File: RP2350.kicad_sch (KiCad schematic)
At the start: 32 parts, among them SW1 SW_Push, SW2 SW_Push, U1 RP2350A, U4 AMS1117-3.3, U5 ABM8-272-T3_C20625731

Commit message: worked on some shit
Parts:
- added Debug: Conn_01x03_Pin, Connector_PinHeader_2.54mm:PinHeader_1x03_P2.54mm_Vertical, symbol Connector:Conn_01x03_Pin
- added R11: 1k, Resistor_SMD:R_0805_2012Metric_Pad1.20x1.40mm_HandSolder, symbol Device:R
- added SW3: SW_Push, Button_Switch_SMD:SW_SPST_EVQPE1, symbol Switch:SW_Push
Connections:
- net BOOT: now also R11.1
- net GND: now also Debug.2 (Pin_2), SW3.1
- net XOUT: now also C9.1
- net SWCLK: now reaches U1.24 (SWCLK)
- net SWCLK: now also Debug.1 (Pin_1)
- net SWDIO: now reaches U1.25 (SWDIO)
- net SWDIO: now also Debug.3 (Pin_3)
- new net: R11.2, SW3.2
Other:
- note added: "Boot"
- note added: "Osc"
- note added: "Reset"
- moved on the sheet: C10, C7, C9, R4, R5, SW1, SW2, U5

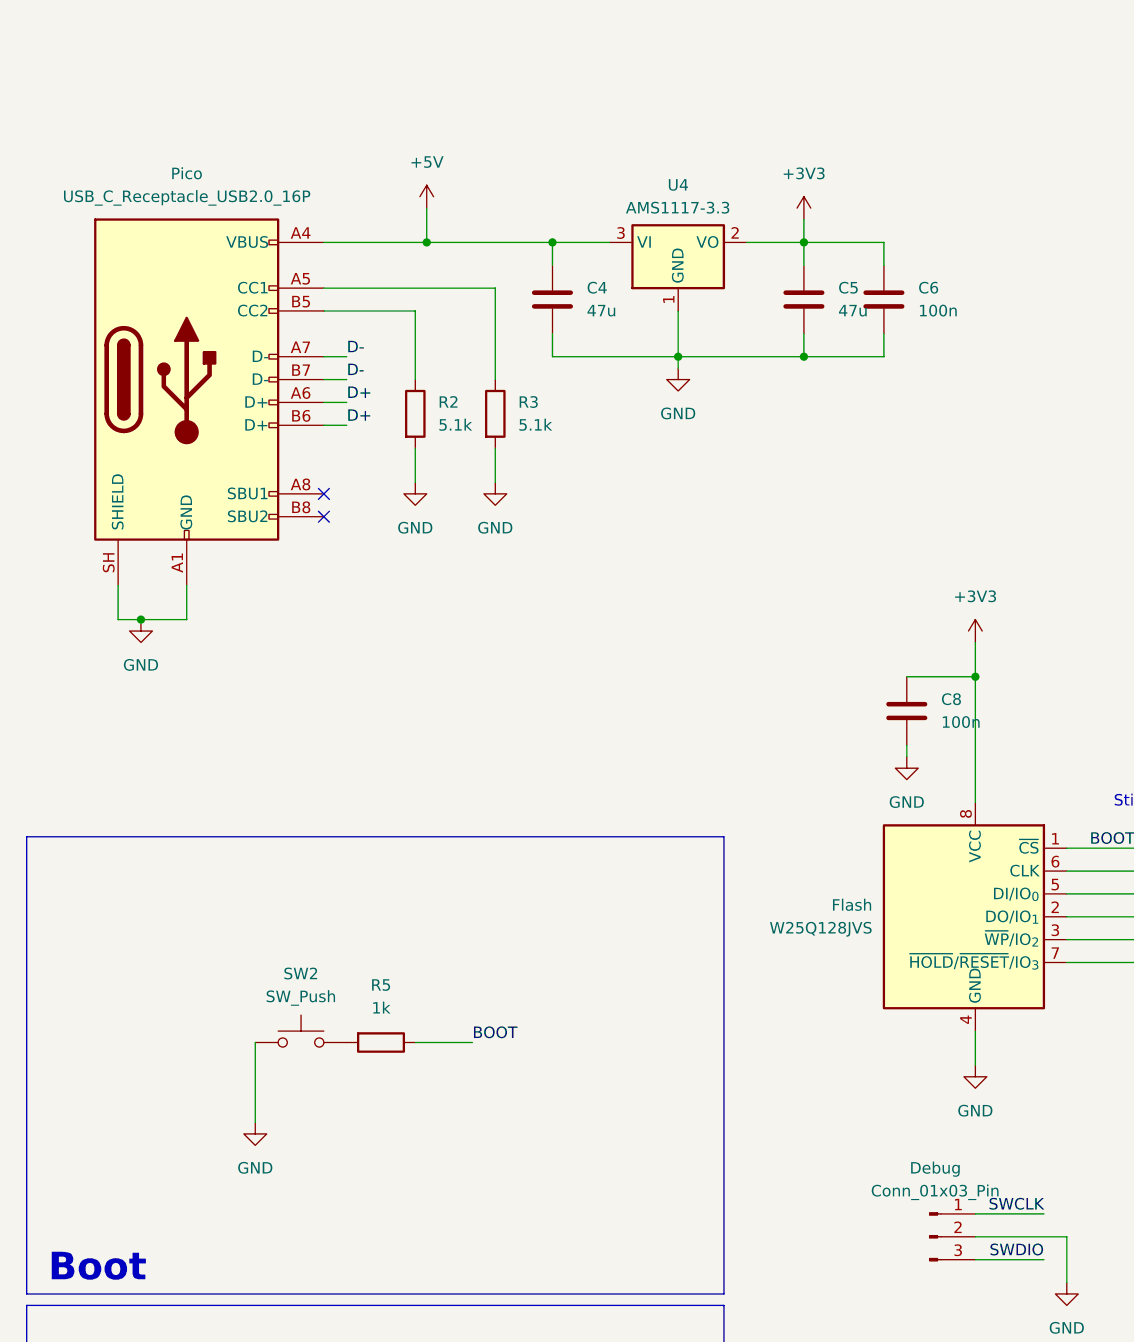
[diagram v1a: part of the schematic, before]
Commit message: added some lcsc part numbers
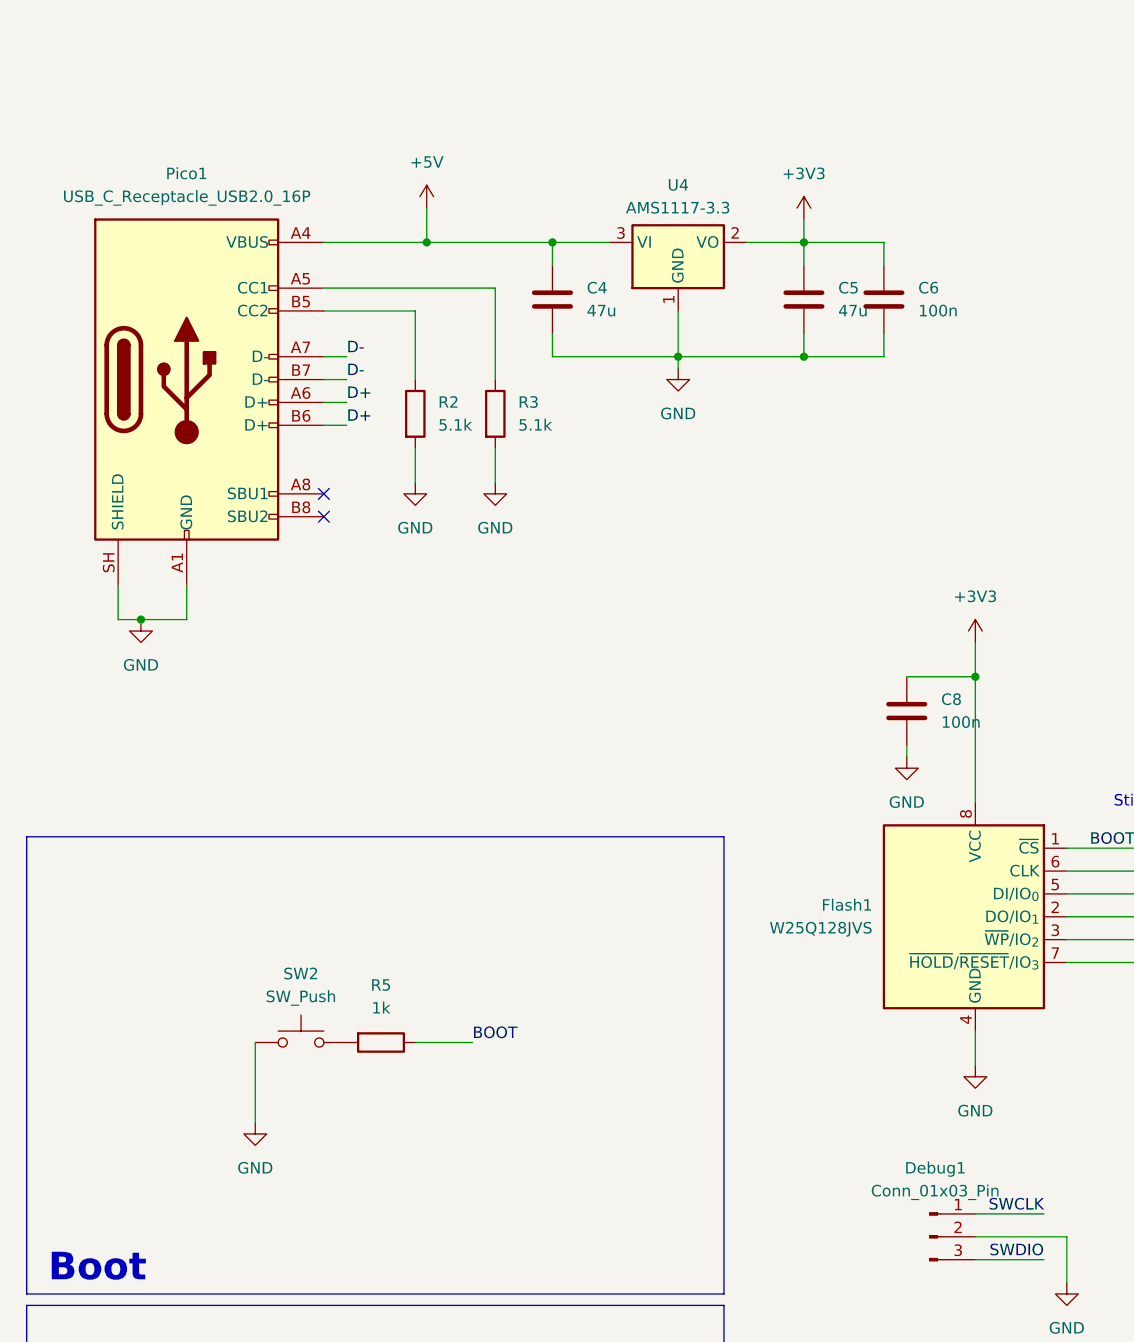
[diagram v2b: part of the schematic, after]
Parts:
- renumbered Debug to Debug1, Flash to Flash1, Pico to Pico1
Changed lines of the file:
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@@
 		(in_pos_files yes)
 		(dnp no)
-		(property "Reference" "Flash"
+		(property "Reference" "Flash1"
 			(at 106.68 101.5999 0)
 			(show_name no)
@@
 			(project "TheDevBoard"
 				(path "/962e0ac6-7545-4a58-b6cb-cae1d23e787f/83027dc2-8dcc-4189-b732-ecb78df2ee53"
-					(reference "Flash")
+					(reference "Flash1")
 					(unit 1)
 				)
@@
 		(dnp no)
 		(fields_autoplaced yes)
-		(property "Reference" "Debug"
+		(property "Reference" "Debug1"
 			(at 113.665 130.81 0)
 			(show_name no)
@@
 			(project "TheDevBoard"
 				(path "/962e0ac6-7545-4a58-b6cb-cae1d23e787f/83027dc2-8dcc-4189-b732-ecb78df2ee53"
-					(reference "Debug")
+					(reference "Debug1")
 					(unit 1)
 				)
@@
 		(dnp no)
 		(fields_autoplaced yes)
-		(property "Reference" "Pico"
+		(property "Reference" "Pico1"
 			(at 30.48 20.32 0)
 			(show_name no)
@@
 			(project "TheDevBoard"
 				(path "/962e0ac6-7545-4a58-b6cb-cae1d23e787f/83027dc2-8dcc-4189-b732-ecb78df2ee53"
-					(reference "Pico")
+					(reference "Pico1")
 					(unit 1)
 				)

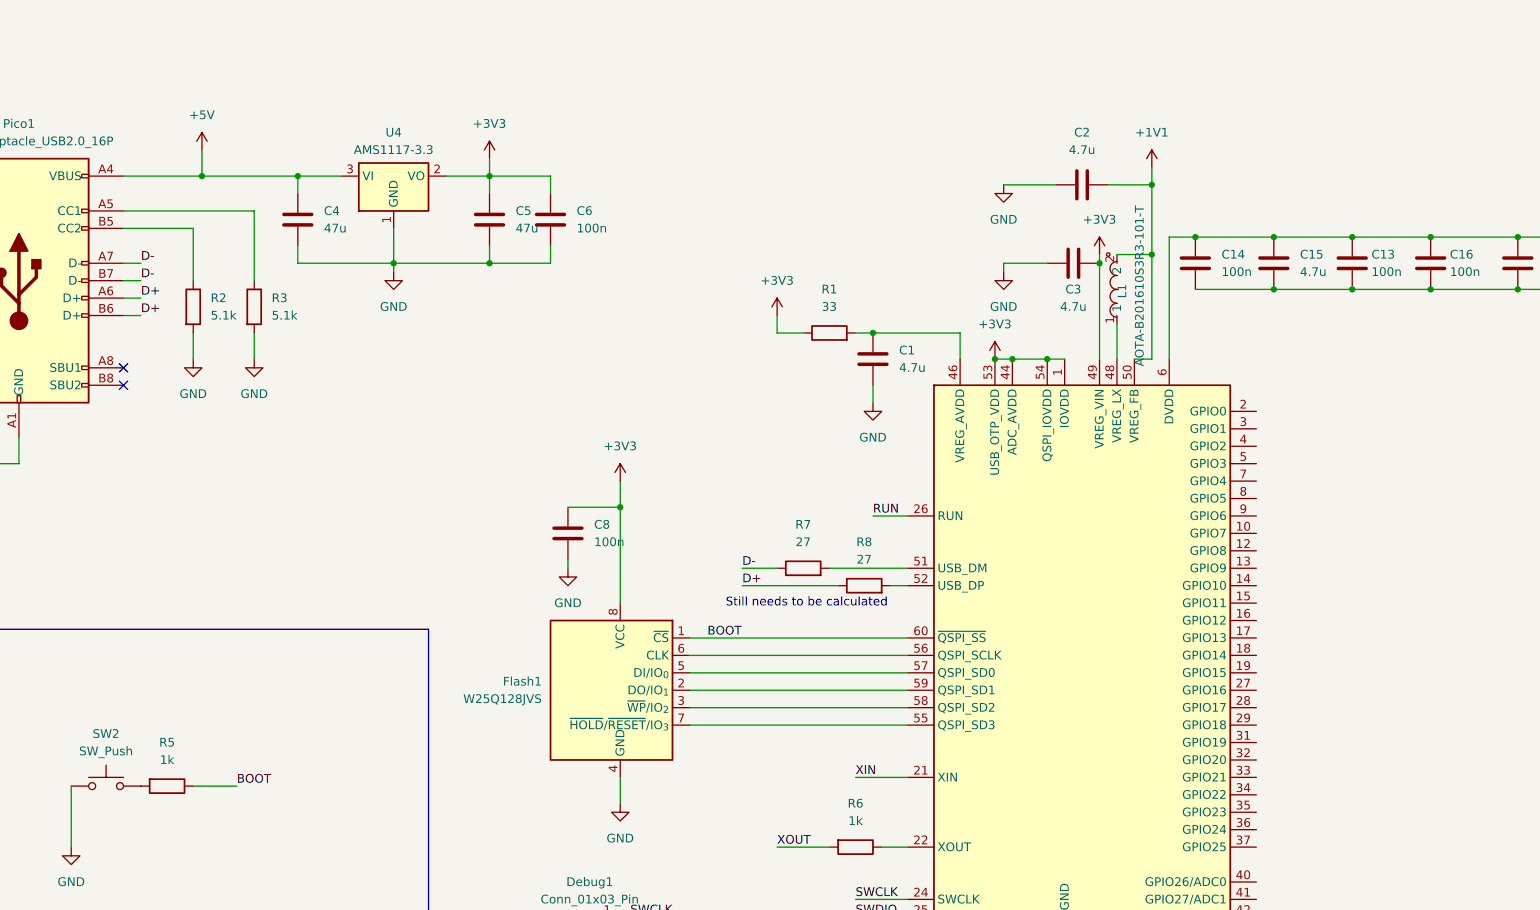
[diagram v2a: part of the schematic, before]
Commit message: created esp32 s3 mini connection to rp2350 added SD card Routed them together
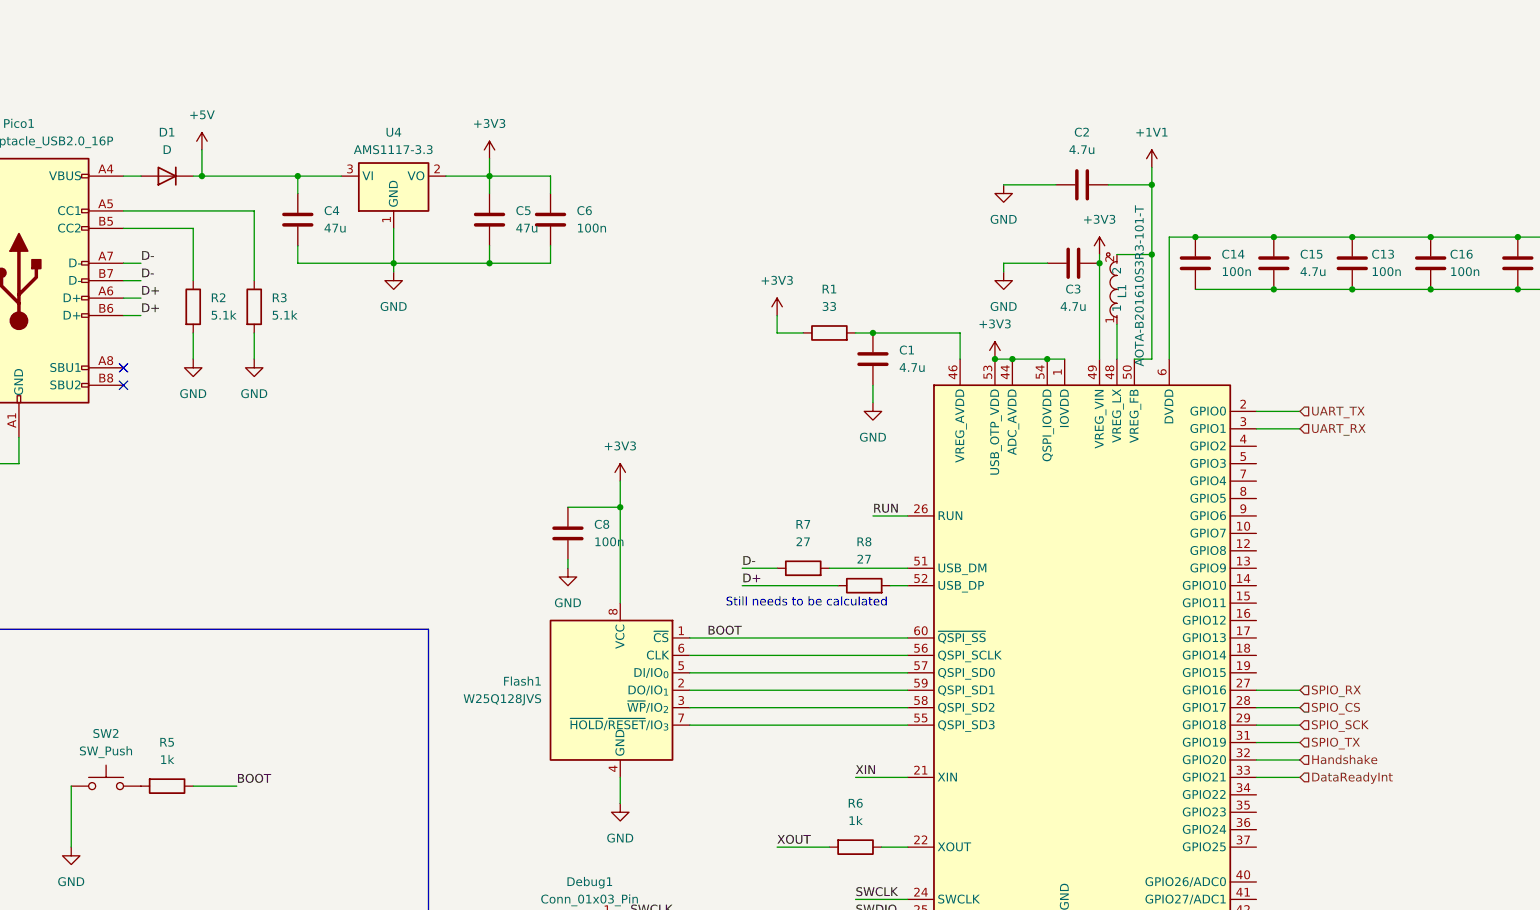
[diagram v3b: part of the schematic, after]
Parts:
- added D1: D, Diode_SMD:D_0805_2012Metric, symbol Device:D
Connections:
- net +5V: now also D1.1 (K); no longer Pico1.A4 (VBUS), Pico1.A9 (VBUS), Pico1.B4 (VBUS), Pico1.B9 (VBUS)
- net UART_TX: now reaches U1.2 (GPIO0)
- net SPIO_RX: now reaches U1.27 (GPIO16)
- net SPIO_CS: now reaches U1.28 (GPIO17)
- net SPIO_SCK: now reaches U1.29 (GPIO18)
- net UART_RX: now reaches U1.3 (GPIO1)
- net SPIO_TX: now reaches U1.31 (GPIO19)
- net Handshake: now reaches U1.32 (GPIO20)
- net DataReadyInt: now reaches U1.33 (GPIO21)
- new net: D1.2 (A), Pico1.A4 (VBUS), Pico1.A9 (VBUS), Pico1.B4 (VBUS), Pico1.B9 (VBUS)

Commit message: generated pdf
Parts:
- removed C4, C5: 47u, Capacitor_SMD:C_0805_2012Metric_Pad1.18x1.45mm_HandSolder, symbol Device:C
- removed C6: 100n, Capacitor_SMD:C_0805_2012Metric_Pad1.18x1.45mm_HandSolder, symbol Device:C
- removed R11: 1k, Resistor_SMD:R_0805_2012Metric_Pad1.20x1.40mm_HandSolder, symbol Device:R
- removed SW3: SW_Push, Button_Switch_SMD:SW_SPST_EVQPE1, symbol Switch:SW_Push
- removed U4: AMS1117-3.3, Package_TO_SOT_SMD:SOT-223-3_TabPin2, symbol Regulator_Linear:AMS1117-3.3
